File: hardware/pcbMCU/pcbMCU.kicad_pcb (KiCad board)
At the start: 2 copper layers, 56.9 x 55.9 mm, 37 parts, among them J1 Conn_01x02, J2 Conn_01x04, J3 Conn_01x03, J4 Conn_01x05, SW1 SW_SPDT, SW2 SW_SPST, U1 AMS1117-3.3, U2 AP62300, U3 ESP32-S3-WROOM-1

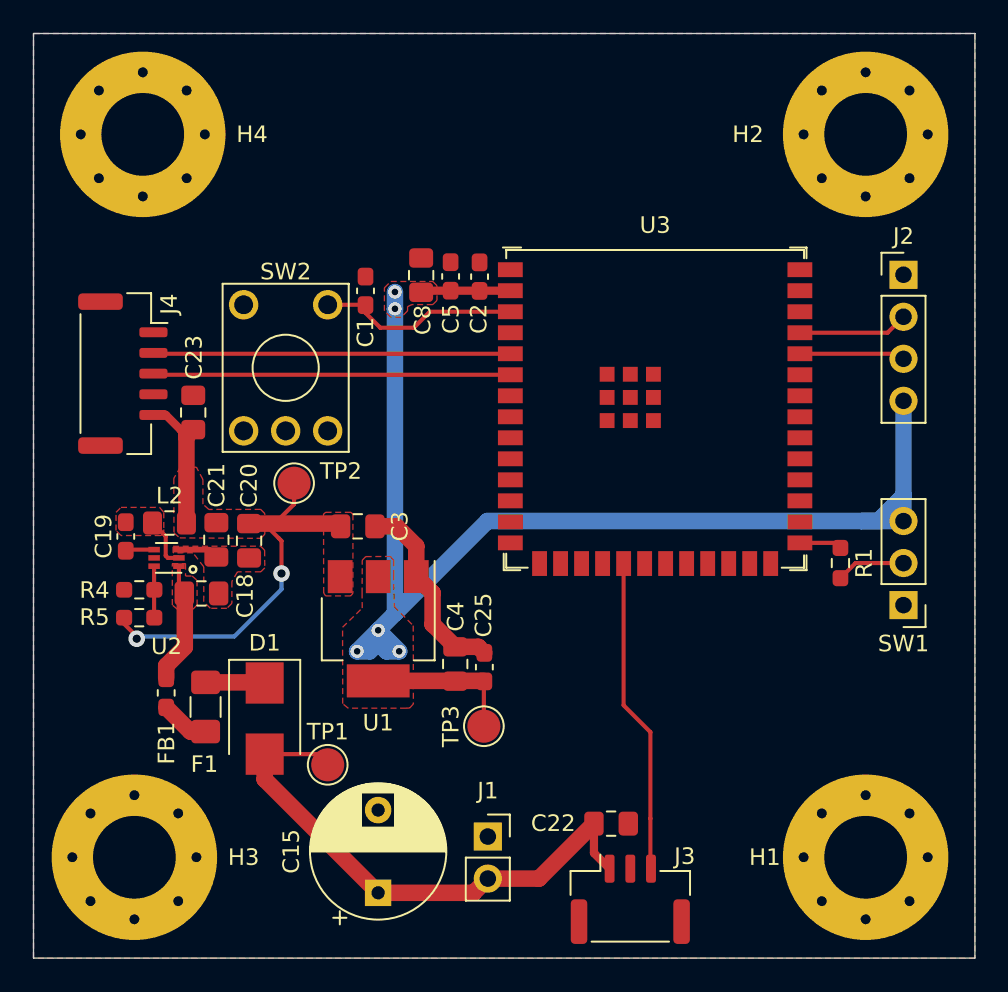
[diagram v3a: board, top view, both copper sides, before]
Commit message: Añadido modelos 3D + Gráficos/descripciones
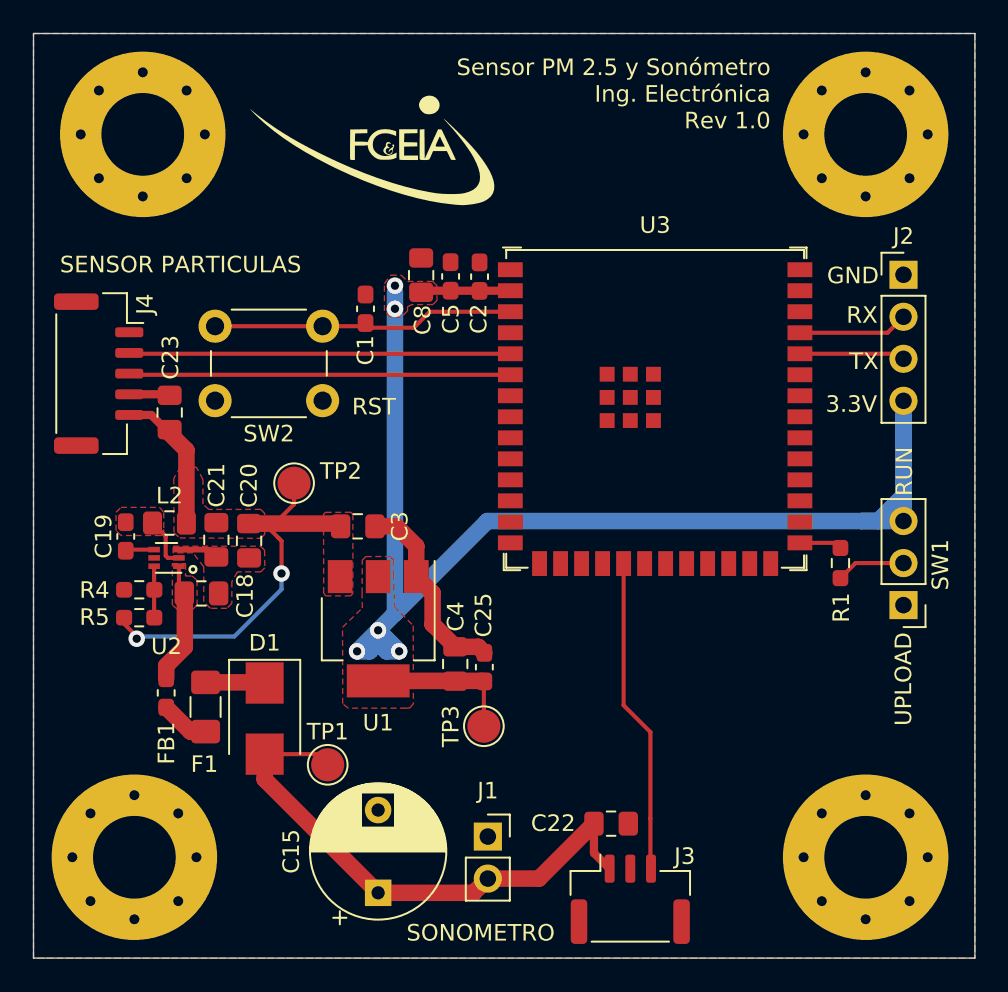
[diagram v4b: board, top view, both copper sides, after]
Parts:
- added G***: LOGO, Project Specific:FCEIA_Logo, F.Cu at (45.2, 49.0)
- SW2: footprint Button_Switch_THT:KSA_Tactile_SPST -> Button_Switch_THT:SW_PUSH_6mm
- moved SW2 7.51 mm to (42.4, 63.8), turned to 180 degrees
- moved J4 1.46 mm to (28.8, 62.2)
- moved C23 1.42 mm to (33.1, 64.6)
- moved C1 1.08 mm to (45.0, 58.3)
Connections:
- H1 pad 1: GND -> (no net)
- H2 pad 1: GND -> (no net)
- H4 pad 1: GND -> (no net)
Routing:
- net EN: track 12.3 -> 18.4 mm
- net GND: track 14.4 -> 16.7 mm
- net SDA_SP: track 21.6 -> 23.1 mm
- net SCL_SP: track 21.6 -> 23.1 mm
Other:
- board text added: "3.3V"
- board text added: "GND"
- board text added: "RST"
- board text added: "RUN"
- board text added: "RX"
- board text added: "SENSOR PARTICULAS"
- board text added: "SONOMETRO"
- board text added: "Sensor PM 2.5 y Sonómetro Ing. Electrónica Rev 1.0"
- board text added: "TX"
- board text added: "UPLOAD"
